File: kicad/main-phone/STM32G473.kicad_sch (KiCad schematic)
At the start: 33 parts, among them J7301 SPARE-IO (DNP), T1 NTCG164KF104FT1, U13 STM32G473VCT6, X1 ABM3-8_000MHZ-D2Y-T, X3 XKXEL89CII-SUAYLC-32_768K

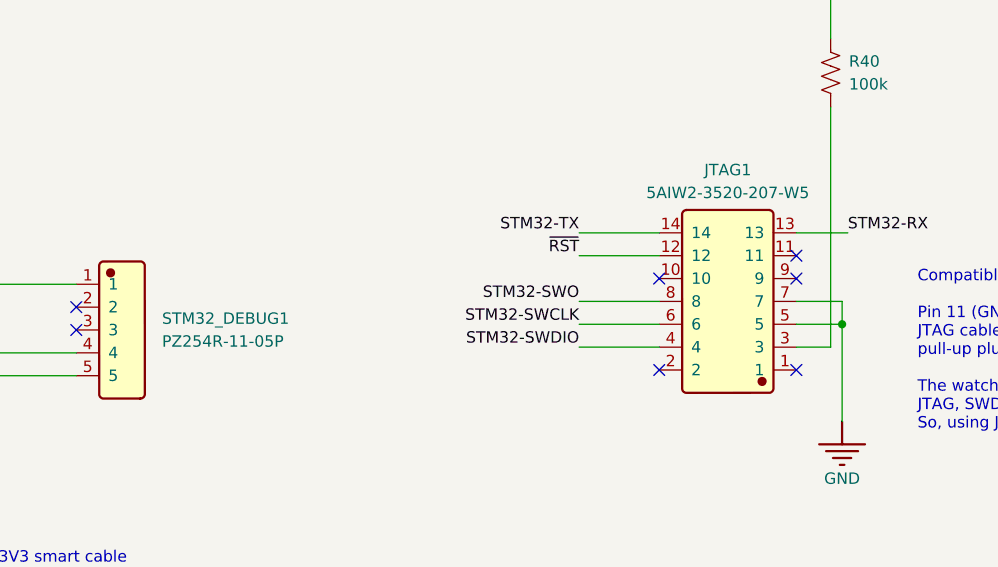
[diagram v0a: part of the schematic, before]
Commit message: main-phone: vertical debug headers (STM32_DEBUG1, JTAG1), reached from the top
- STM32_DEBUG1: PZ254R-11-05P right angle -> PZ254V-11-05P vertical (C492404)
- JTAG1: 2x7 1.27 mm right angle -> SMD vertical PZ1.27-2x7PTP-L7.2 (C55099228), STDC14 pinout
- JLCImport: PZ1_27-2X7P-TP symbol, footprint, 3D model
- same pin numbers; netlist and ERC unchanged otherwise; docs updated

Co-Authored-By: Claude Opus 5.5 (1M context) <noreply@anthropic.com>
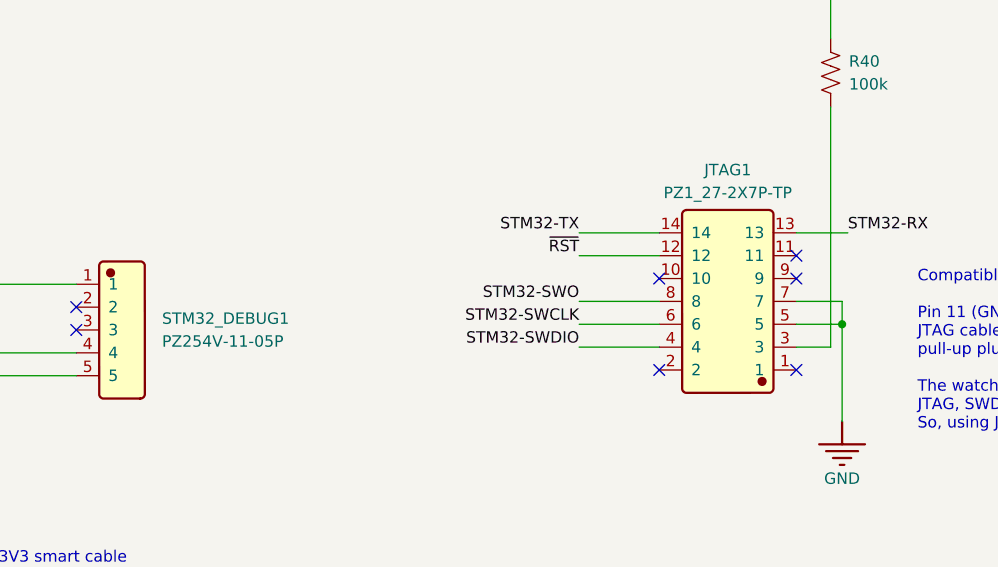
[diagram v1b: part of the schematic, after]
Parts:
- JTAG1: value 5AIW2-3520-207-W5 -> PZ1_27-2X7P-TP; footprint JLCImport:5AIW2-3520-207-W5 -> JLCImport:PZ1_27-2X7P-TP; symbol JLCImport:5AIW2-3520-207-W5 -> JLCImport:PZ1_27-2X7P-TP; LCSC C52120825 -> C55099228; Manufacturer SAMZO -> SHOU HAN; Manufacturer Part 5AIW2-3520-207-W5 -> PZ1.27-2x7PTP-L7.2
- STM32_DEBUG1: value PZ254R-11-05P -> PZ254V-11-05P; footprint Connector_PinHeader_2.54mm:PinHeader_1x05_P2.54mm_Horizontal -> Connector_PinHeader_2.54mm:PinHeader_1x05_P2.54mm_Vertical; LCSC C492413 -> C492404; Manufacturer Part PZ254R-11-05P -> PZ254V-11-05P
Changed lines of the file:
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@@
 	)
 	(symbol
-		(lib_id "JLCImport:5AIW2-3520-207-W5")
+		(lib_id "JLCImport:PZ1_27-2X7P-TP")
 		(at 257.81 316.865 180)
 		(unit 1)
@@
 			)
 		)
-		(property "Value" "5AIW2-3520-207-W5"
+		(property "Value" "PZ1_27-2X7P-TP"
 			(at 257.81 304.8 0)
 			(show_name no)
@@
 			)
 		)
-		(property "Footprint" "JLCImport:5AIW2-3520-207-W5"
+		(property "Footprint" "JLCImport:PZ1_27-2X7P-TP"
 			(at 257.81 316.865 0)
 			(hide yes)
@@
 			)
 		)
-		(property "Datasheet" "https://atta.szlcsc.com/upload/public/pdf/source/20251027/16F2AFD684EAEF36731369EE7B609875.pdf"
+		(property "Datasheet" "https://www.lcsc.com/datasheet/C55099228.pdf"
 			(at 257.81 316.865 0)
 			(hide yes)
@@
 			)
 		)
-		(property "Description" "-40℃~+105℃ 1.27mm 1.27mm 1.5mm 14P 1A 2 2mm 500V Black Brass Gold Pin Header 弯插,P=1.27mm Pin Headers ROHS"
+		(property "Description" "2x7 1.27 mm SMD vertical header, STDC14 pinout (ST-LINK V3), reached from the top under a cover"
 			(at 257.81 316.865 0)
 			(hide yes)
@@
 			)
 		)
-		(property "LCSC" "C52120825"
+		(property "LCSC" "C55099228"
 			(at 257.81 316.865 0)
 			(hide yes)
@@
 			)
 		)
-		(property "Manufacturer" "SAMZO"
+		(property "Manufacturer" "SHOU HAN"
 			(at 257.81 316.865 0)
 			(hide yes)
@@
 			)
 		)
-		(property "Manufacturer Part" "5AIW2-3520-207-W5"
+		(property "Manufacturer Part" "PZ1.27-2x7PTP-L7.2"
 			(at 257.81 316.865 0)
 			(hide yes)
@@
 			)
 		)
-		(property "Value" "PZ254R-11-05P"
+		(property "Value" "PZ254V-11-05P"
 			(at 194.945 321.3099 0)
 			(show_name no)
@@
 			)
 		)
-		(property "Footprint" "Connector_PinHeader_2.54mm:PinHeader_1x05_P2.54mm_Horizontal"
+		(property "Footprint" "Connector_PinHeader_2.54mm:PinHeader_1x05_P2.54mm_Vertical"
 			(at 190.5 320.04 0)
 			(hide yes)
@@
 			)
 		)
-		(property "Datasheet" "https://www.lcsc.com/datasheet/lcsc_datasheet_2003191006_XFCN-PZ254R-11-05P_C492413.pdf"
+		(property "Datasheet" "https://www.lcsc.com/datasheet/C492404.pdf"
 			(at 190.5 320.04 0)
 			(hide yes)
@@
 			)
 		)
-		(property "Description" "1x5 right-angle 0.1in header (same part as LIDAR2)"
+		(property "Description" "1x5 vertical 0.1in header (UART console), reached from the top under a cover"
 			(at 190.5 320.04 0)
 			(hide yes)
@@
 			)
 		)
-		(property "LCSC" "C492413"
+		(property "LCSC" "C492404"
 			(at 190.5 320.04 0)
 			(hide yes)
@@
 			)
 		)
-		(property "Manufacturer Part" "PZ254R-11-05P"
+		(property "Manufacturer Part" "PZ254V-11-05P"
 			(at 190.5 320.04 0)
 			(hide yes)

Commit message: main-phone: free MCU pins; 2x11 spare header with UART and I2C
- LiDAR rail enable joins ~VM-VBAT-EN (PE10); PD9 freed
- IMU FSYNC/INT2 go to J7301 instead of the MCU; FSYNC 100k pull-down (R7601); PD4/PD7 freed
- one open-drain ToF interrupt (PD12) for both VL53L7s and the side VL53L0X; PC8/PE2 freed
- right VL53L7 LPn held up by R7307, no MCU pin; PE8 freed
- IMU moved from I2C2 to I2C4 (R18/R72 not fitted); PA8/PA9 freed;
  R7315 keeps PA9 (UCPD DBCC1) pulled up for dead-battery Rd on CC1
- PWR_EN moved PC10 -> PD7; PC10/PC11 are a spare UART
- J7301 2x6 -> 2x11: 3.3 V, 5 V, I2C4, UART, 12 spare GPIO, IMU FSYNC/INT2, GND
- docs: SPEC, main-phone and side-sensor READMEs

Co-Authored-By: Claude Opus 5.5 <noreply@anthropic.com>
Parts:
- removed J7301: SPARE-IO (DNP), Connector_PinHeader_2.54mm:PinHeader_2x06_P2.54mm_Vertical, symbol Connector_Generic:Conn_02x06_Odd_Even
- added J7301: SPARE-IO (DNP), Connector_PinHeader_2.54mm:PinHeader_2x11_P2.54mm_Vertical, symbol Connector_Generic:Conn_02x11_Odd_Even
- added R7315: 10k, Resistor_SMD:R_0603_1608Metric, symbol Device:R_US
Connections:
- net GND: now also J7301.21 (Pin_21), J7301.22 (Pin_22)
- net I2C4_SCL: now also J7301.3 (Pin_3)
- net I2C4_SDA: now also J7301.4 (Pin_4)
- net IMU-FSYNC: now also J7301.19 (Pin_19); no longer U13.86 (PD4)
- net IMU-INT#2: now also J7301.20 (Pin_20); no longer U13.89 (PD7)
- net SPARE-PA10: now also J7301.7 (Pin_7)
- net SPARE-PC9: now also J7301.9 (Pin_9)
- net SPARE-PE4: now also J7301.10 (Pin_10)
- net SPARE-PE5: now also J7301.11 (Pin_11)
- net SPARE-PE6: now also J7301.8 (Pin_8)
- net USB_PWR_EN: now also U13.89 (PD7); no longer U13.79 (PC10)
- net VCC-3V3-REG: now also J7301.1 (Pin_1), R7315.1
- net VCC-5V-REG: now also J7301.2 (Pin_2)
- net I2C2_SCL renamed SPARE-PA9
- net SPARE-PA9: now also J7301.16 (Pin_16), R7315.2
- net I2C2_SDA renamed SPARE-PA8
- net SPARE-PA8: now also J7301.15 (Pin_15)
- net LIDAR_EN renamed SPARE-PD9
- net SPARE-PD9: now also J7301.12 (Pin_12)
- net SIDE-PROXI-GPIO-R renamed SPARE-PE2
- net SPARE-PE2: now also J7301.18 (Pin_18)
- net SPARE-PC11 renamed SPARE-PC11-RX
- net SPARE-PC11-RX: now also J7301.6 (Pin_6)
- net VL-R-INT renamed SPARE-PC8
- net SPARE-PC8: now also J7301.17 (Pin_17)
- net VL-R-LPn renamed SPARE-PE8
- net SPARE-PE8: now also J7301.13 (Pin_13)
- new net SPARE-PC10-TX: J7301.5 (Pin_5), U13.79 (PC10)
- new net SPARE-PD4: J7301.14 (Pin_14), U13.86 (PD4)
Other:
- note added: "J7301 spare I/O: 0.1in 2x11 pads, do not fit (zero height). 1 VCC-3V3-REG (sensor rail), 2 VCC-5V-REG, 21/22 GND. 3/4 I2C4 SCL/SDA (shared with the ToF, side sensor and IMU; 2.2k pull-ups). 5/6 UART PC10 TX / PC11 RX (UART4 or USART3). 7-18 spare GPIO; 12/13 PD9/PE8 are ADC-capable. 19/20 IMU FSYNC/INT2 (FSYNC: 100k pull-down on the IMU sheet). SWO (PB3) on JTAG1 is a spare when not tracing."
- note added: "R7315: PA9 = UCPD DBCC1. High during reset turns on the dead-battery Rd on CC1 (PB6)."
- note removed: "J7301 spare I/O: 0.1in 2x6 pads, do not fit (zero height). 1 VCC-3V3-REG (sensor rail), 2 VCC-5V-REG, 3/4 I2C4 SCL/SDA (shared with ToF/side sensors, 2.2k pull-ups), 5-10 spare GPIO, 11/12 GND."

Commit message: Cliff sensor board (IR333-A + PT333-3B, no lenses); main board drops the Roomba harness
- kicad/cliff-sensor: new board, fitted 6x. Narrow-beam 5 mm IR LED and black-lens
  phototransistor, 18 mm apart, tilted so the beams cross at the floor (tilt sets the
  reference distance). 150R LED resistor, SH 4-pin vertical (ZX-SH1.0-4PLT). Refs 85xx.
- main-phone CLIFF sheet: BUMP_CLIFF1 (Roomba 2x8 harness), R30, R35 removed; six SH 4-pin
  connectors CLIFF-LF1..RR1; Q7701 (AO3400) switches all cliff LEDs from CLIFF_LED_EN
  (R7703 pull-down); 47k pull-ups incl. new R7701/R7702 for cliff LM (PD9) / RM (PE8)
- STM32 sheet: PD9/PE8 carry cliff LM/RM (global labels), also on J7301 12/13
- JLCImport: IR333-A, PT333-3B, ZX-SH1_0-4PLT
- docs: cliff board README, SPEC, READMEs

Co-Authored-By: Claude Opus 5.5 <noreply@anthropic.com>
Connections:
- net SPARE-PD9 renamed CLIFF-LM-Q+
- net SPARE-PE8 renamed CLIFF-RM-Q+
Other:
- note added: "J7301 spare I/O: 0.1in 2x11 pads, do not fit (zero height). 1 VCC-3V3-REG (sensor rail), 2 VCC-5V-REG, 21/22 GND. 3/4 I2C4 SCL/SDA (shared with the ToF, side sensor and IMU; 2.2k pull-ups). 5/6 UART PC10 TX / PC11 RX (UART4 or USART3). 7-18 spare GPIO, except 12/13 = cliff LM/RM (PD9/PE8 ADC). 19/20 IMU FSYNC/INT2 (FSYNC: 100k pull-down on the IMU sheet). SWO (PB3) on JTAG1 is a spare when not tr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"
- note removed: "J7301 spare I/O: 0.1in 2x11 pads, do not fit (zero height). 1 VCC-3V3-REG (sensor rail), 2 VCC-5V-REG, 21/22 GND. 3/4 I2C4 SCL/SDA (shared with the ToF, side sensor and IMU; 2.2k pull-ups). 5/6 UART PC10 TX / PC11 RX (UART4 or USART3). 7-18 spare GPIO; 12/13 PD9/PE8 are ADC-capable. 19/20 IMU FSYNC/INT2 (FSYNC: 100k pull-down on the IMU sheet). SWO (PB3) on JTAG1 is a spare when not tracing."
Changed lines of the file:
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@@
 		)
 	)
-	(label "SPARE-PD9"
+	(global_label "CLIFF-LM-Q+"
+		(shape input)
 		(at 272.415 162.56 0)
+		(fields_autoplaced yes)
 		(effects
 			(font
 				(size 1.27 1.27)
 			)
-			(justify left bottom)
+			(justify left)
+		)
+		(property "Intersheetrefs" "${INTERSHEET_REFS}"
+			(at 272.415 162.56 0)
+			(hide yes)
+			(show_name no)
+			(do_not_autoplace no)
+			(effects
+				(font
+					(size 1.27 1.27)
+				)
+				(justify left)
+			)
 		)
 	)
@@
 		)
 	)
-	(label "SPARE-PE8"
+	(global_label "CLIFF-RM-Q+"
+		(shape input)
 		(at 365.76 113.03 180)
+		(fields_autoplaced yes)
 		(effects
 			(font
 				(size 1.27 1.27)
 			)
-			(justify right bottom)
+			(justify right)
+		)
+		(property "Intersheetrefs" "${INTERSHEET_REFS}"
+			(at 365.76 113.03 180)
+			(hide yes)
+			(show_name no)
+			(do_not_autoplace no)
+			(effects
+				(font
+					(size 1.27 1.27)
+				)
+				(justify right)
+			)
 		)
 	)
@@
 		)
 	)
-	(label "SPARE-PD9"
+	(global_label "CLIFF-LM-Q+"
+		(shape input)
 		(at 533.4 195.58 0)
+		(fields_autoplaced yes)
 		(effects
 			(font
 				(size 1.27 1.27)
 			)
-			(justify left bottom)
+			(justify left)
+		)
+		(property "Intersheetrefs" "${INTERSHEET_REFS}"
+			(at 533.4 195.58 0)
+			(hide yes)
+			(show_name no)
+			(do_not_autoplace no)
+			(effects
+				(font
+					(size 1.27 1.27)
+				)
+				(justify left)
+			)
 		)
 	)
@@
 		)
 	)
-	(label "SPARE-PE8"
+	(global_label "CLIFF-RM-Q+"
+		(shape input)
 		(at 510.54 198.12 180)
+		(fields_autoplaced yes)
 		(effects
 			(font
 				(size 1.27 1.27)
 			)
-			(justify right bottom)
+			(justify right)
+		)
+		(property "Intersheetrefs" "${INTERSHEET_REFS}"
+			(at 510.54 198.12 180)
+			(hide yes)
+			(show_name no)
+			(do_not_autoplace no)
+			(effects
+				(font
+					(size 1.27 1.27)
+				)
+				(justify right)
+			)
 		)
 	)
@@
 		)
 	)
-	(text "J7301 spare I/O: 0.1in 2x11 pads, do not fit (zero height).\n1 VCC-3V3-REG (sensor rail), 2 VCC-5V-REG, 21/22 GND.\n3/4 I2C4 SCL/SDA (shared with the ToF, side sensor and IMU; 2.2k pull-ups).\n5/6 UART PC10 TX / PC11 RX (UART4 or USART3). 7-18 spare GPIO;\n12/13 PD9/PE8 are ADC-capable. 19/20 IMU FSYNC/INT2 (FSYNC: 100k\npull-down on the IMU sheet). SWO (PB3) on JTAG1 is a spare when not tracing."
+	(text "J7301 spare I/O: 0.1in 2x11 pads, do not fit (zero height).\n1 VCC-3V3-REG (sensor rail), 2 VCC-5V-REG, 21/22 GND.\n3/4 I2C4 SCL/SDA (shared with the ToF, side sensor and IMU; 2.2k pull-ups).\n5/6 UART PC10 TX / PC11 RX (UART4 or USART3). 7-18 spare GPIO, except\n12/13 = cliff LM/RM (PD9/PE8 ADC). 19/20 IMU FSYNC/INT2 (FSYNC: 100k\npull-down on the IMU sheet). SWO (PB3) on JTAG1 is a spare when not tracing."
 		(exclude_from_sim no)
 		(at 492.76 236.22 0)
